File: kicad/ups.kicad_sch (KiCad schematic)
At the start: 64 parts, among them J1 Input, J2 Output, J3 Batt, J4 Conn_01x01, J5 Conn_01x02_Pin, J6 2S_MID, Q1 IRF7324, Q2 AO3401A, Q3 AO3401A, Q4 FDS6890A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

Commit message: Add PCB and Gerbers
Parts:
- added H1, H2: MountingHole_Pad, MountingHole:MountingHole_3.2mm_M3_DIN965_Pad, symbol Mechanical:MountingHole_Pad
- J5: value Conn_01x02_Pin -> NTC
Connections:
- net Earth: now also Q4.3 (S2), H1.1, H2.1; no longer Q4.1 (S1)
- net PG: now also R15.2; no longer D4.1 (K)
- net ST1: now also R13.2; no longer D2.1 (K)
- net ST2: now also R14.2; no longer D3.1 (K)
- net at C5.1, Q1.1 (S1), Q1.3 (S2)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: now also D2.2 (A), D3.2 (A), D4.2 (A); no longer R13.1, R14.1, R15.1
- net at C1.1, C2.1, C3.1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: now also Q4.7 (D1), Q4.8 (D1); no longer Q4.5 (D2), Q4.6 (D2)
- net at U1.P19 (LODRV): now also Q4.4 (G2); no longer Q4.2 (G1)
- net at C9.2, L1.1, U1.P20 (PH): now also Q4.1 (S1), Q4.5 (D2), Q4.6 (D2); no longer Q4.3 (S2), Q4.7 (D1), Q4.8 (D1)
- net at U1.P21 (HIDRV): now also Q4.2 (G1); no longer Q4.4 (G2)
- new net: D4.1 (K), R15.1
- new net: D3.1 (K), R14.1
- new net: D2.1 (K), R13.1
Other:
- moved on the sheet: D2, D3, D4, Q4A, Q4B, R13, R14, R15

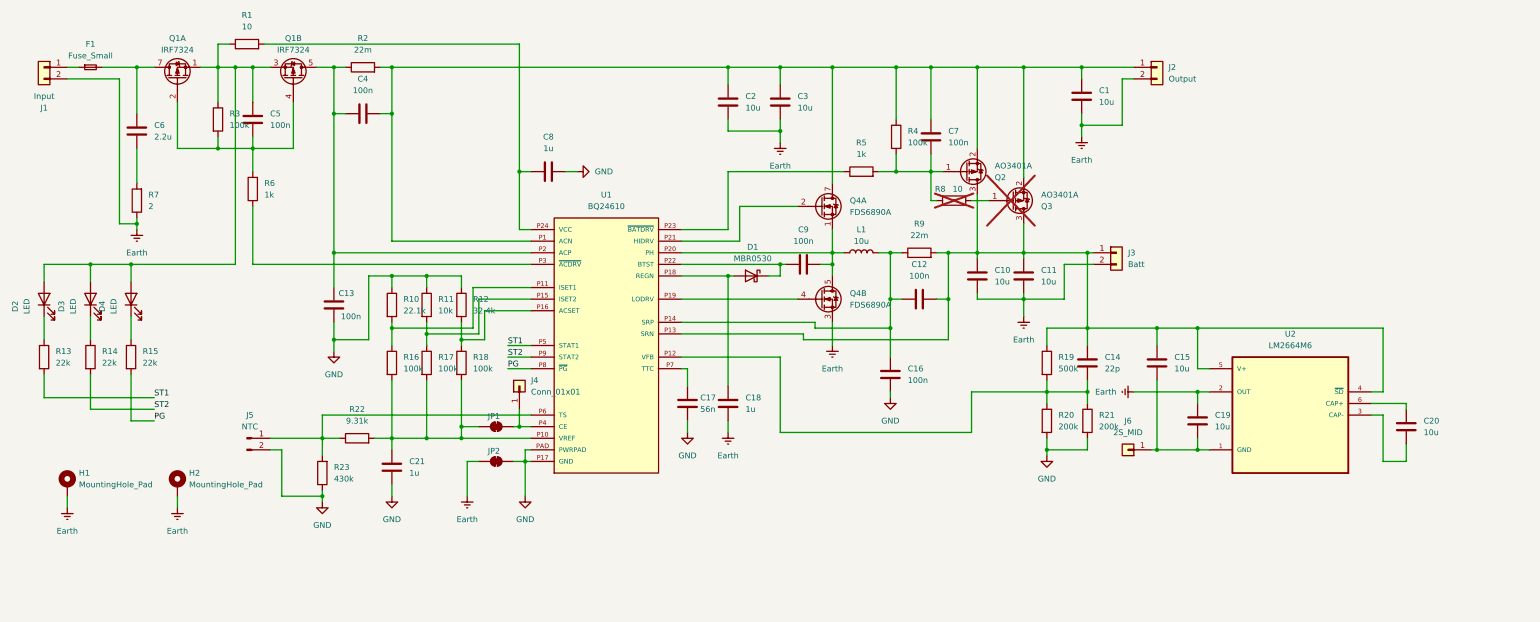
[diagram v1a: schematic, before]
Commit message: Add recharge threshold control
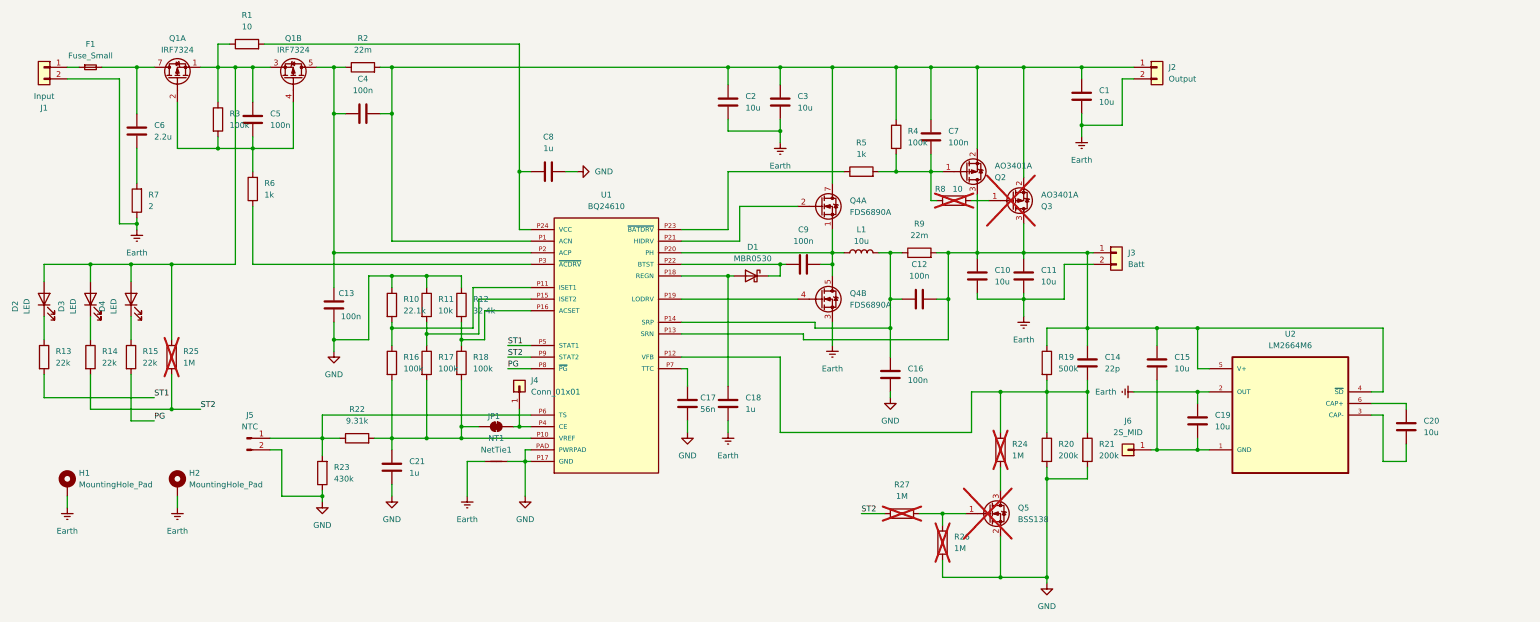
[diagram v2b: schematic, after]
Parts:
- removed JP2: SolderJumper_2_Bridged, Jumper:SolderJumper-2_P1.3mm_Bridged_RoundedPad1.0x1.5mm, symbol Jumper:SolderJumper_2_Bridged
- added NT1: NetTie1, NetTie:NetTie-2_SMD_Pad2.0mm, symbol Device:NetTie_2
- added Q5: BSS138, Package_TO_SOT_SMD:SOT-23, symbol Transistor_FET:BSS138
- added R24: 1M, Resistor_SMD:R_0805_2012Metric_Pad1.20x1.40mm_HandSolder, symbol Device:R
- added R25, R26, R27: 1M, Resistor_SMD:R_0603_1608Metric, symbol Device:R
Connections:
- net Earth: now also NT1.2
- net GND: now also NT1.1, Q5.2 (S), R26.2
- net ST2: now also R25.2, R27.1
- net at C14.2, R19.2, R20.1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: now also R24.1
- net at C5.1, D2.2 (A), D3.2 (A)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: now also R25.1
- new net: Q5.1 (G), R26.1, R27.2
- new net: Q5.3 (D), R24.2
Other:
- moved on the sheet: R20, R21

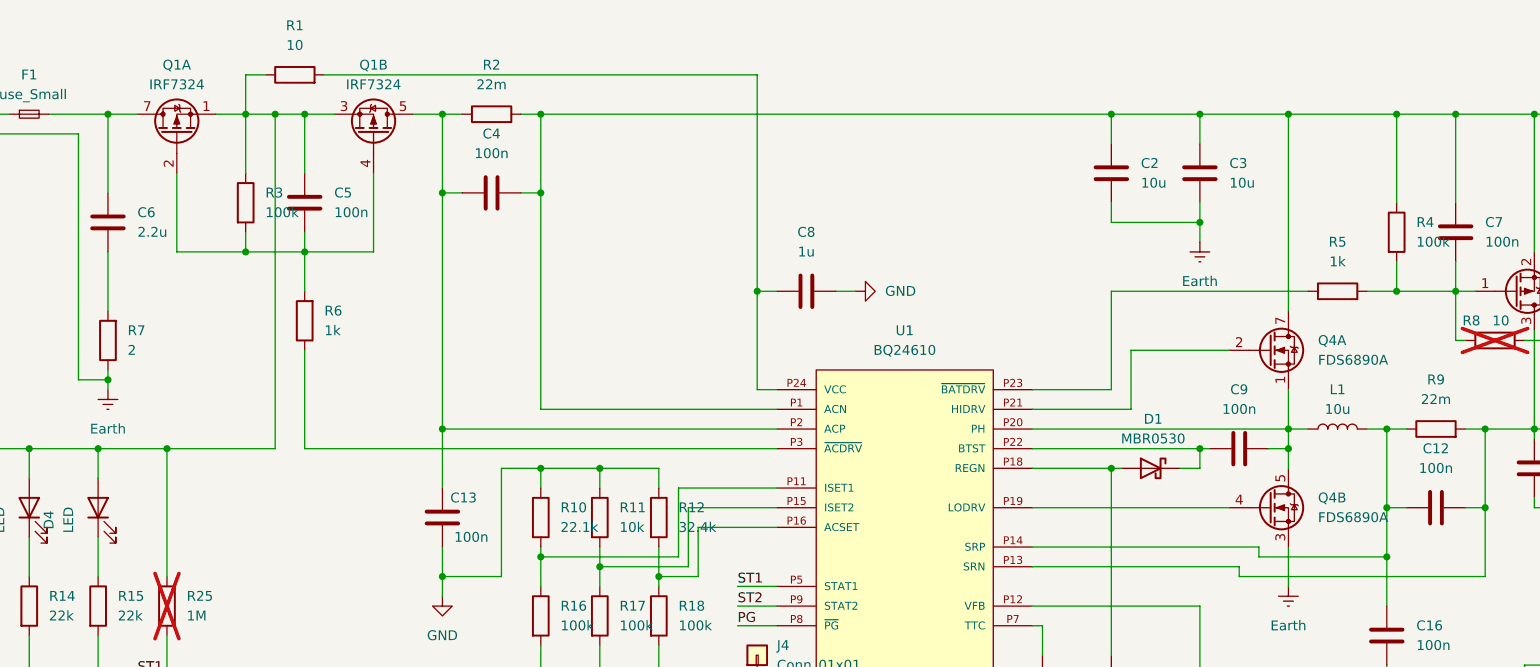
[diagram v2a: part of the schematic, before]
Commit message: Update part names, minor fix in the ground plane
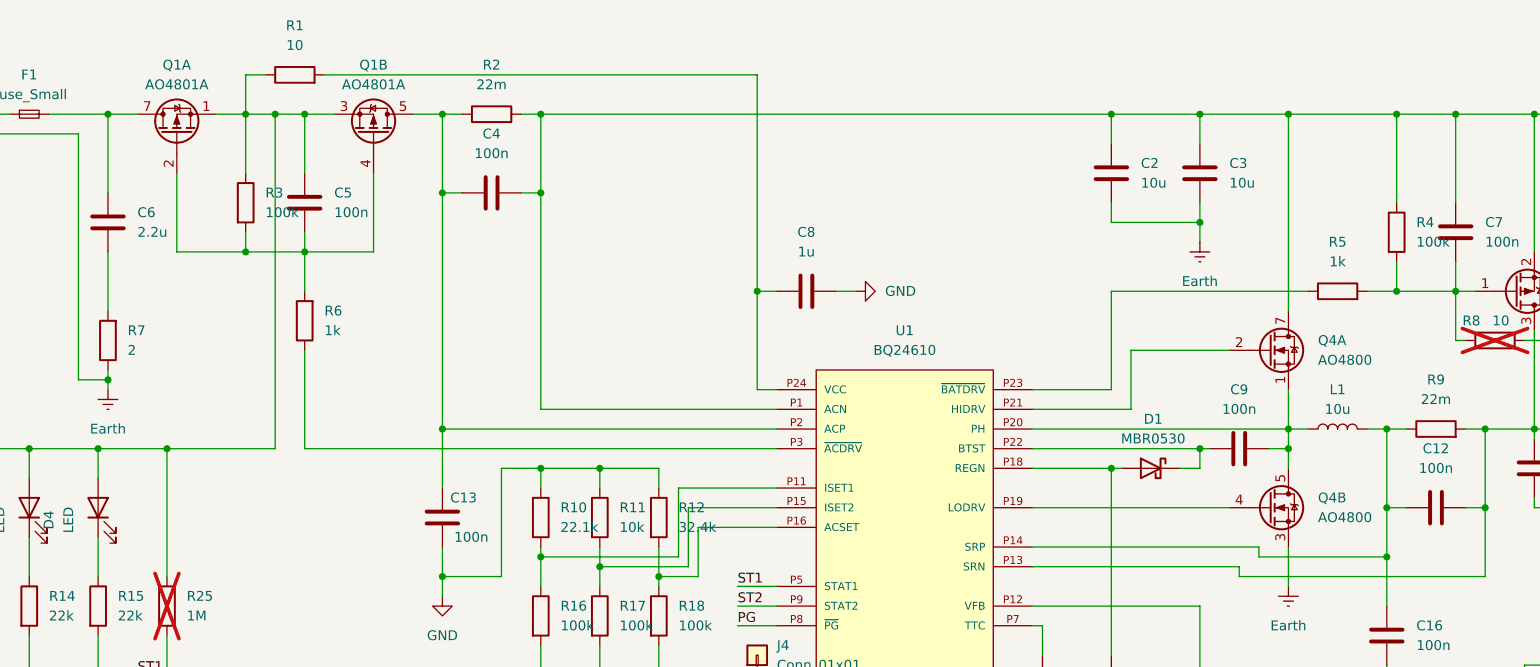
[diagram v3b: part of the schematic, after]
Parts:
- Q1: value IRF7324 -> AO4801A
- Q4: value FDS6890A -> AO4800
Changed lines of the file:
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@@
 			)
 		)
-		(property "Value" "IRF7324"
+		(property "Value" "AO4801A"
 			(at 100.33 91.44 90)
 			(effects
@@
 			)
 		)
-		(property "Value" "FDS6890A"
+		(property "Value" "AO4800"
 			(at 247.65 126.9999 0)
 			(effects
@@
 			)
 		)
-		(property "Value" "FDS6890A"
+		(property "Value" "AO4800"
 			(at 247.65 147.3199 0)
 			(effects
@@
 			)
 		)
-		(property "Value" "IRF7324"
+		(property "Value" "AO4801A"
 			(at 125.73 91.44 90)
 			(effects

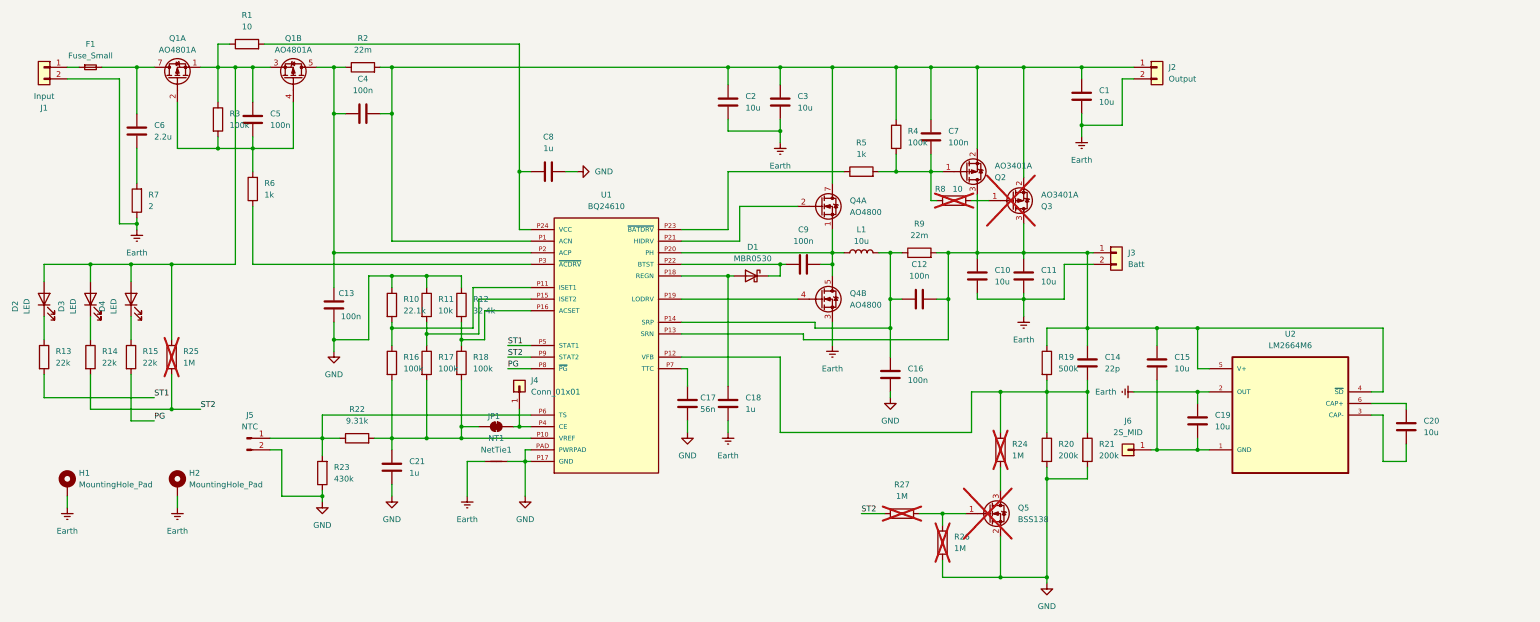
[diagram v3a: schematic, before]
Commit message: Add equation formulas to schematics
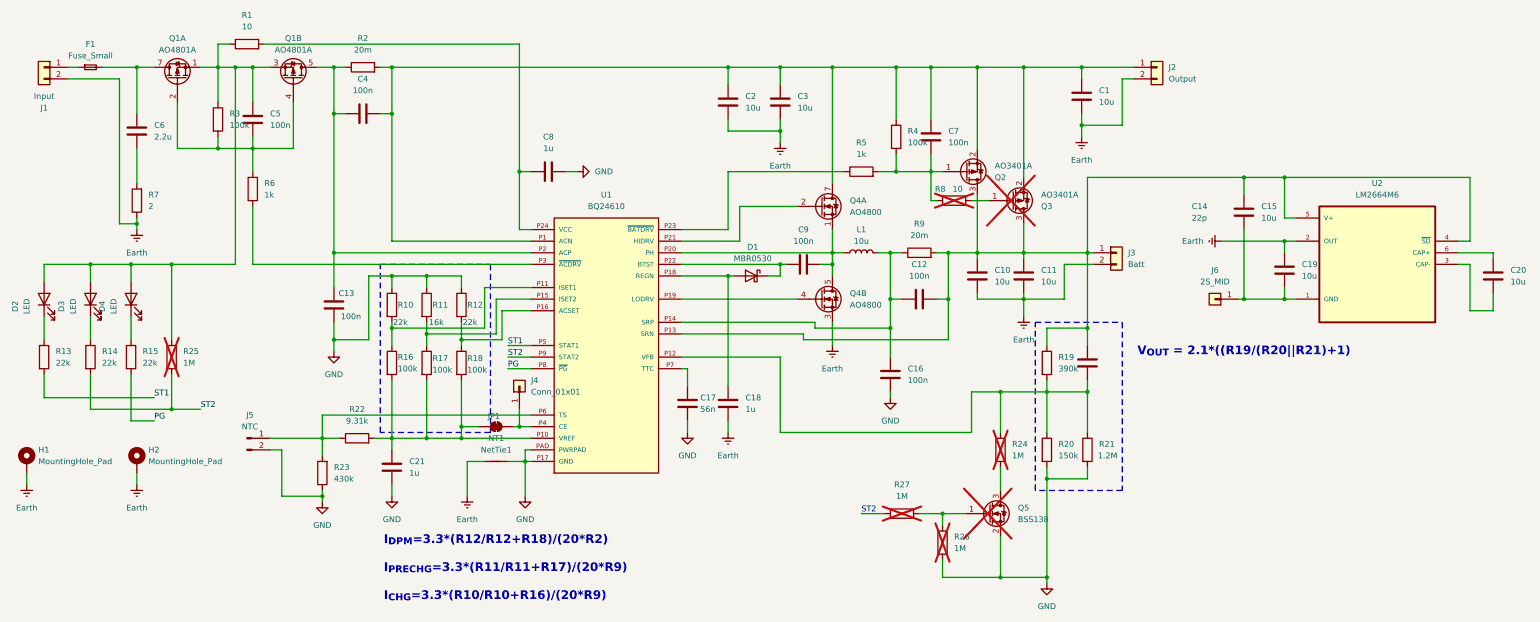
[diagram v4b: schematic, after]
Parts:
- R10: value 22.1k -> 22k
- R11: value 10k -> 16k
- R12: value 32.4k -> 22k
- R19: value 500k -> 390k
- R2, R9: value 22m -> 20m
- R20: value 200k -> 150k
- R21: value 200k -> 1.2M
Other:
- note added: "I_{DPM}=3.3*(R12/R12+R18)/(20*R2) I_{PRECHG}=3.3*(R11/R11+R17)/(20*R9) I_{CHG}=3.3*(R10/R10+R16)/(20*R9)"
- note added: "V_{OUT} = 2.1*((R19/(R20||R21)+1)"
- moved on the sheet: C15, C19, C20, H1, H2, J6, U2

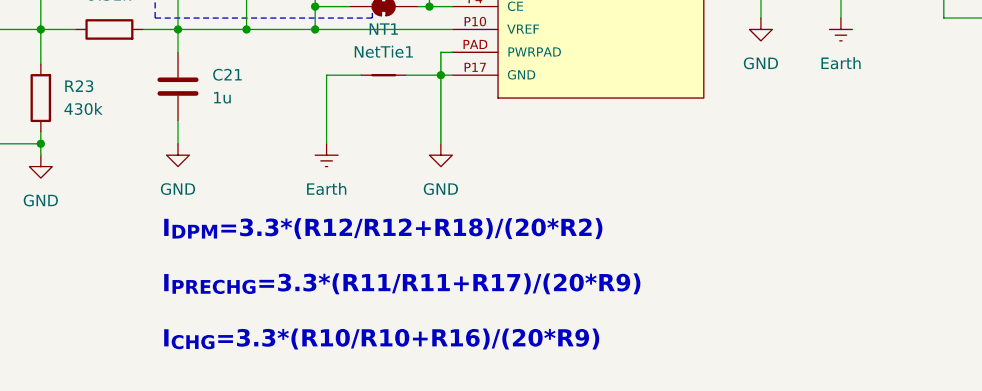
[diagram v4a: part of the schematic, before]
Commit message: sch: Fix precharge equation
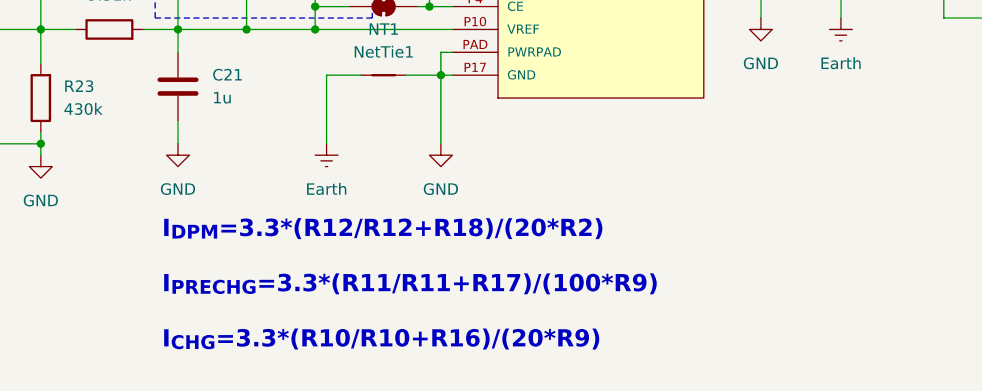
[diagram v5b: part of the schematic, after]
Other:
- note added: "I_{DPM}=3.3*(R12/R12+R18)/(20*R2) I_{PRECHG}=3.3*(R11/R11+R17)/(100*R9) I_{CHG}=3.3*(R10/R10+R16)/(20*R9)"
- note removed: "I_{DPM}=3.3*(R12/R12+R18)/(20*R2) I_{PRECHG}=3.3*(R11/R11+R17)/(20*R9) I_{CHG}=3.3*(R10/R10+R16)/(20*R9)"
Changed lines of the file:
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@@
 		)
 	)
-	(text "I_{DPM}=3.3*(R12/R12+R18)/(20*R2)\n\nI_{PRECHG}=3.3*(R11/R11+R17)/(20*R9)\n\nI_{CHG}=3.3*(R10/R10+R16)/(20*R9)\n"
+	(text "I_{DPM}=3.3*(R12/R12+R18)/(20*R2)\n\nI_{PRECHG}=3.3*(R11/R11+R17)/(100*R9)\n\nI_{CHG}=3.3*(R10/R10+R16)/(20*R9)\n"
 		(exclude_from_sim no)
 		(at 145.542 204.978 0)
